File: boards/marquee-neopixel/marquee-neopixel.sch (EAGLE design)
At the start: 86 parts, among them U1 ATTINY85-20SU

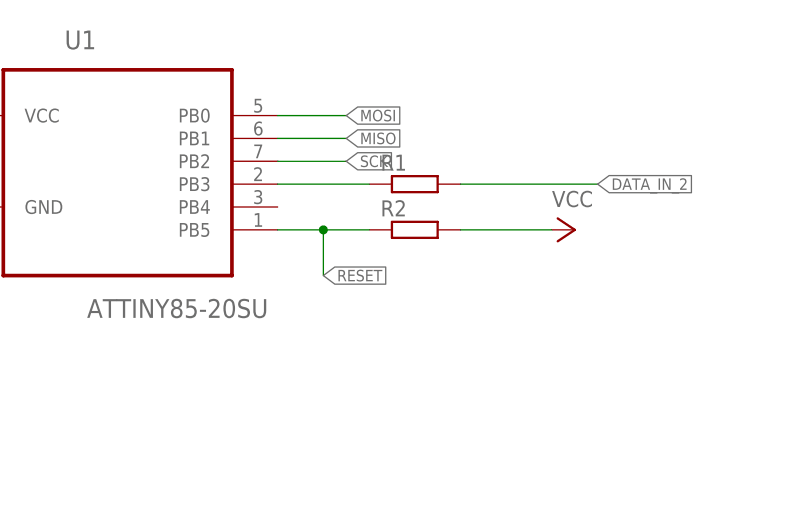
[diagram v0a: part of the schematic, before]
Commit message: adds example boards for common circuits
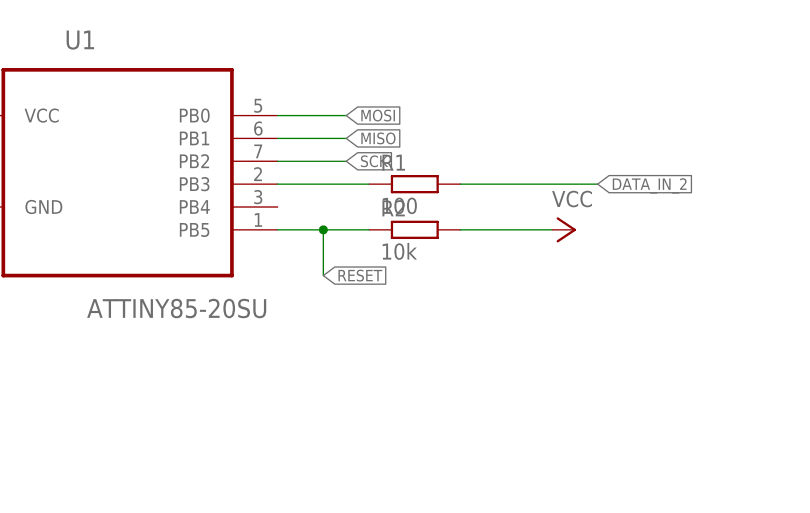
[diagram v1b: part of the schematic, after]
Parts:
- R1: value (none) -> 100
- R2: value (none) -> 10k
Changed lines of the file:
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@@
 <?xml version="1.0" encoding="utf-8"?>
 <!DOCTYPE eagle SYSTEM "eagle.dtd">
-<eagle version="8.5.2">
+<eagle version="8.6.1">
 <drawing>
 <settings>
@@
 </part>
 <part name="C38" library="rcl" library_urn="urn:adsk.eagle:library:334" deviceset="C-US" device="C0603" package3d_urn="urn:adsk.eagle:package:23616/2" value="0.1uf"/>
-<part name="R1" library="eagle-ltspice" library_urn="urn:adsk.eagle:library:217" deviceset="R" device="R0603" package3d_urn="urn:adsk.eagle:package:13302/1"/>
+<part name="R1" library="eagle-ltspice" library_urn="urn:adsk.eagle:library:217" deviceset="R" device="R0603" package3d_urn="urn:adsk.eagle:package:13302/1" value="100"/>
 <part name="C41" library="rcl" library_urn="urn:adsk.eagle:library:334" deviceset="CPOL-US" device="153CLV-0605" package3d_urn="urn:adsk.eagle:package:23398/1" value="47uf"/>
 <part name="P+77" library="supply1" library_urn="urn:adsk.eagle:library:371" deviceset="VCC" device="">
@@
 <part name="C39" library="rcl" library_urn="urn:adsk.eagle:library:334" deviceset="C-US" device="C0603" package3d_urn="urn:adsk.eagle:package:23616/2" value="4.7uf"/>
 <part name="C44" library="rcl" library_urn="urn:adsk.eagle:library:334" deviceset="C-US" device="C0603" package3d_urn="urn:adsk.eagle:package:23616/2" value="4.7uf"/>
-<part name="R2" library="eagle-ltspice" library_urn="urn:adsk.eagle:library:217" deviceset="R" device="R0603" package3d_urn="urn:adsk.eagle:package:13302/1"/>
+<part name="R2" library="eagle-ltspice" library_urn="urn:adsk.eagle:library:217" deviceset="R" device="R0603" package3d_urn="urn:adsk.eagle:package:13302/1" value="10k"/>
 <part name="P+81" library="supply1" library_urn="urn:adsk.eagle:library:371" deviceset="VCC" device=""/>
 <part name="JP2" library="pinhead" library_urn="urn:adsk.eagle:library:325" deviceset="PINHD-2X3" device="" package3d_urn="urn:adsk.eagle:package:22462/2"/>
